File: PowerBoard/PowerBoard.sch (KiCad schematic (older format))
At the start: 25 parts

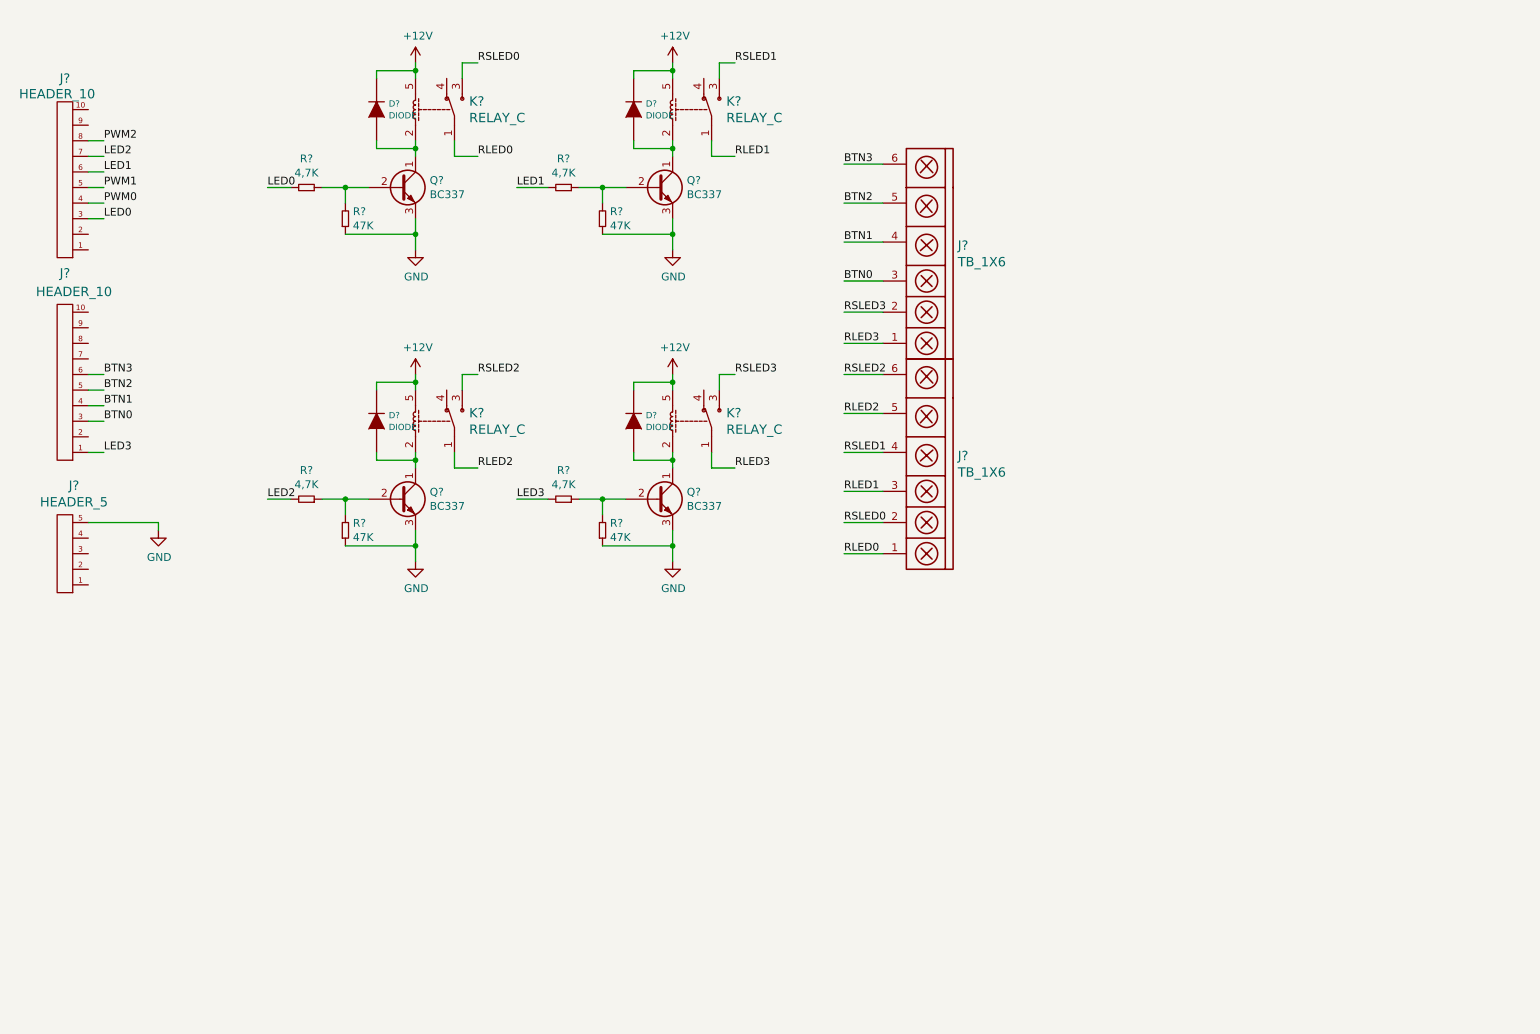
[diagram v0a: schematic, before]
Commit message: Diseño de la placa al 70%. Considero nuevas alternativas a este proyecto.
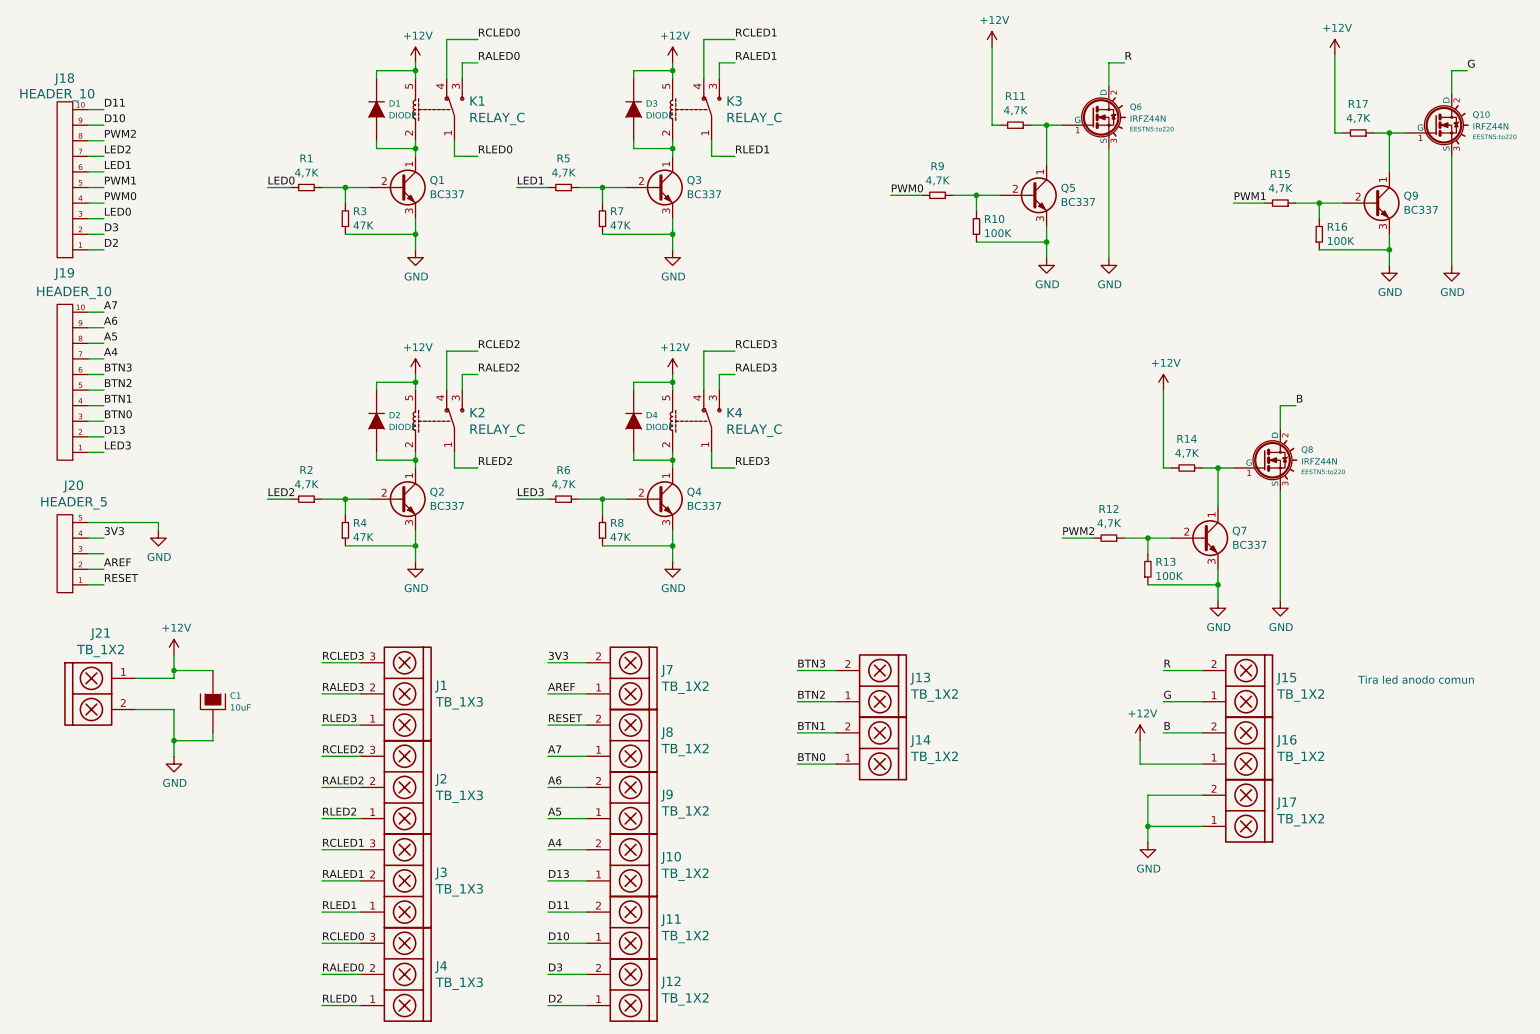
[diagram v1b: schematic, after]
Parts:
- removed J? (x2): TB_1X6, symbol EESTN5:TB_1X6
- added C1: 10uF, EESTN5:CAP_ELEC_5x11mm, symbol EESTN5:CAPAPOL
- added J1, J2, J3, J4: TB_1X3, EESTN5:BORNERA3, symbol EESTN5:TB_1X3
- added J10, J11, J12, J13, J14, J15, J16, J17, J21, J7, J8, J9: TB_1X2, EESTN5:BORNERA2, symbol EESTN5:TB_1X2
- added Q10, Q6, Q8: IRFZ44N, EESTN5:to220, symbol EESTN5:IRFZ44N
- added Q5, Q7, Q9: BC337, EESTN5:to92, symbol EESTN5:BC337
- added R10, R13, R16: 100K, EESTN5:R_1206, symbol EESTN5:R
- added R11, R14, R17: 4,7K, EESTN5:RES0.3, symbol EESTN5:R
- added R12, R15, R9: 4,7K, EESTN5:R_1206, symbol EESTN5:R
- D1, D2, D3, D4: renamed from D?; footprint (none) -> EESTN5:DO-41
- J18, J19: renamed from J?; footprint (none) -> EESTN5:Pin_Header_Straight_1x10
- J20: renamed from J?; footprint (none) -> EESTN5:Pin_Header_5
- K1, K2, K3, K4: renamed from K?; footprint (none) -> EESTN5:Relay_C
- Q1, Q2, Q3, Q4: renamed from Q?; footprint EESTN5:TO-92 -> EESTN5:to92
- R1, R2, R3, R4, R5, R6, R7, R8: renamed from R?; footprint (none) -> EESTN5:RES0.3
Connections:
- net +12V: now also C1.1, J16.1, J21.1, R11.2, R14.2, R17.2
- net BTN0: now also J14.1
- net BTN1: now also J14.2
- net BTN2: now also J13.1
- net BTN3: now also J13.2
- net GND: now also C1.2, J17.1, J17.2, J21.2, Q10.3 (S), Q5.3 (E), Q6.3 (S), Q7.3 (E), Q8.3 (S), Q9.3 (E), R10.1, R13.1, R16.1
- net PWM0: now also R9.2
- net PWM1: now also R15.2
- net PWM2: now also R12.2
- net RLED0: now also J4.1
- net RLED1: now also J3.1
- net RLED2: now also J2.1
- net RLED3: now also J1.1
- net D2: now reaches J18.1
- net D2: now also J12.1
- net D11: now reaches J18.10
- net D11: now also J11.2
- net D3: now reaches J18.2
- net D3: now also J12.2
- net D10: now reaches J18.9
- net D10: now also J11.1
- net A7: now reaches J19.10
- net A7: now also J8.1
- net D13: now reaches J19.2
- net D13: now also J10.1
- net A4: now reaches J19.7
- net A4: now also J10.2
- net A5: now reaches J19.8
- net A5: now also J9.1
- net A6: now reaches J19.9
- net A6: now also J9.2
- net RESET: now reaches J20.1
- net RESET: now also J8.2
- net AREF: now reaches J20.2
- net AREF: now also J7.1
- net 3V3: now reaches J20.4
- net 3V3: now also J7.2
- net RCLED0: now reaches K1.4
- net RCLED0: now also J4.3
- net RCLED2: now reaches K2.4
- net RCLED2: now also J2.3
- net RCLED1: now reaches K3.4
- net RCLED1: now also J3.3
- net RCLED3: now reaches K4.4
- net RCLED3: now also J1.3
- net RSLED0 renamed RALED0
- net RALED0: now also J4.2
- net RSLED1 renamed RALED1
- net RALED1: now also J3.2
- net RSLED2 renamed RALED2
- net RALED2: now also J2.2
- net RSLED3 renamed RALED3
- net RALED3: now also J1.2
- new net: Q5.1 (C), Q6.1 (G), R11.1
- new net: Q5.2 (B), R10.2, R9.1
- new net: Q10.1 (G), Q9.1 (C), R17.1
- new net: Q9.2 (B), R15.1, R16.2
- new net: Q7.1 (C), Q8.1 (G), R14.1
- new net: Q7.2 (B), R12.1, R13.2
- new net B: J16.2, Q8.2 (D)
- new net G: J15.1, Q10.2 (D)
- new net R: J15.2, Q6.2 (D)
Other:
- note added: "Tira led anodo comun\n"
